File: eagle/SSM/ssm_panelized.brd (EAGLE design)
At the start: 73 x 33.6 mm, 23 parts, among them IC1 4051N, IC2 MCP604P

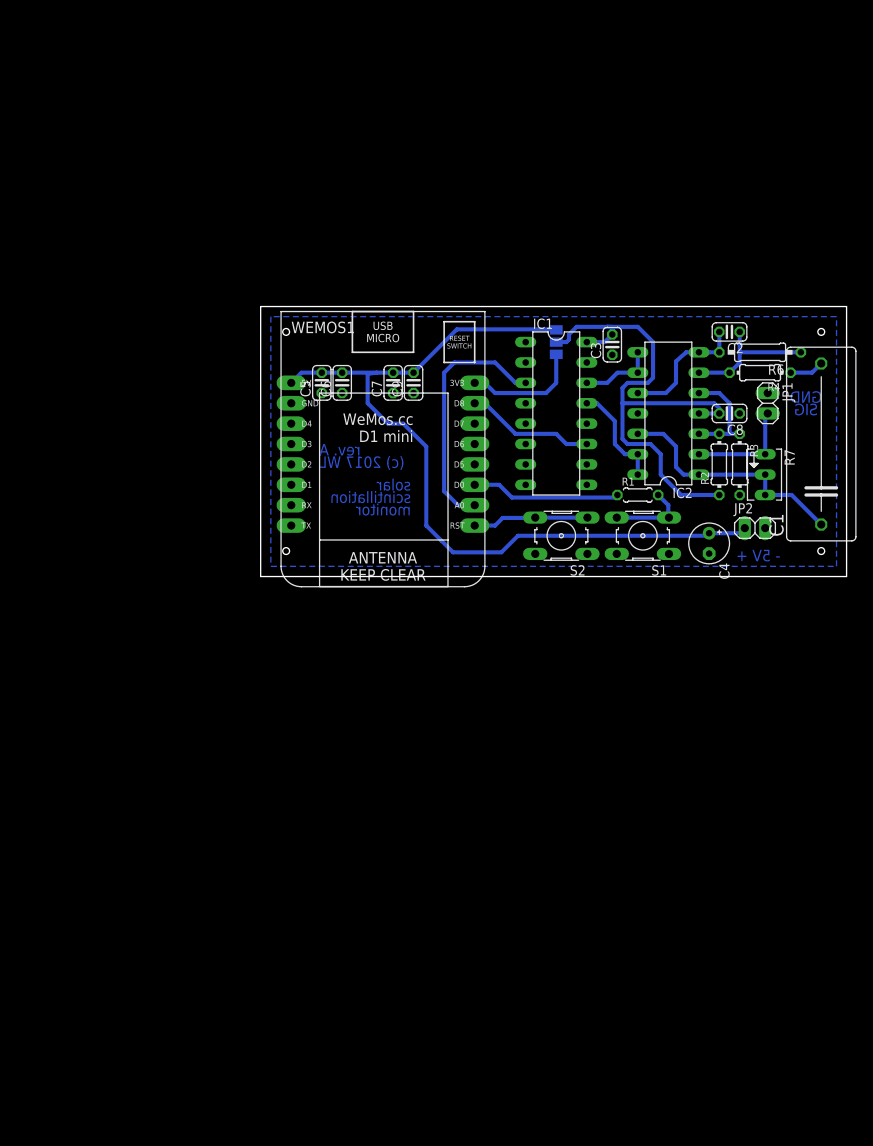
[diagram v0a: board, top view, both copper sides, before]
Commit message: panelized version
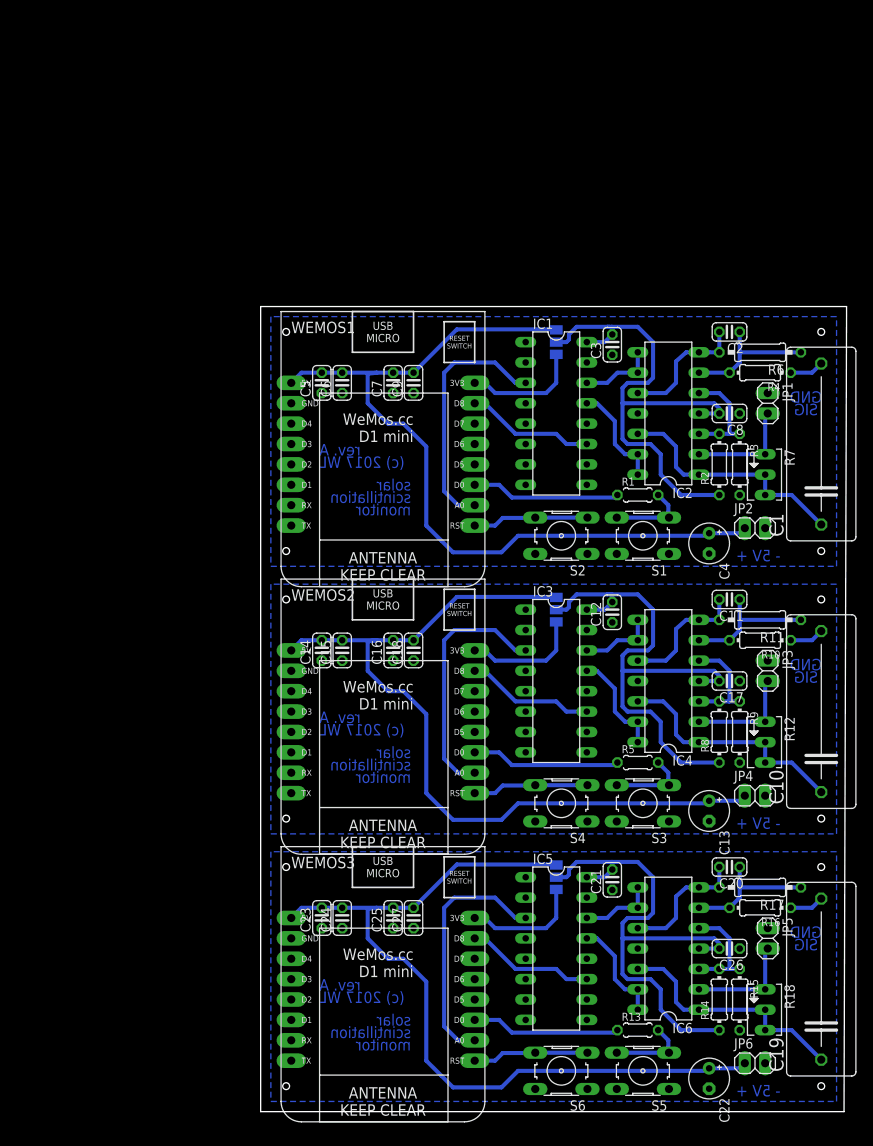
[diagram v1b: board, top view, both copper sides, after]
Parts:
- added C10, C19: 3.3u, Cap:C225-087X210
- added C11, C14, C20, C23: 20p, rcl:C025-024X044
- added C12, C15, C16, C17, C18, C21, C24, C25, C26, C27: 120p, rcl:C025-024X044
- added C13, C22: 470u, rcl:E2,5-5
- added IC3, IC5: 4051N, 40xx:DIL16
- added IC4, IC6: MCP604P, linear:DIL14
- added JP3, JP5: SENS, pinhead:1X02
- added JP4, JP6: PWR, pinhead:1X02
- added R10, R16: 47k, resistor:0204/7
- added R11, R17: 20M, rcl:0207/10
- added R12, R18: 1k, pot:B64Y
- added R13, R5: 470, rcl:0204/5
- added R14, R15, R8, R9: 10k, resistor:0204/7
- added S3, S5: FLS, switch-omron:B3F-10XX
- added S4, S6: RST, switch-omron:B3F-10XX
- added SJ2, SJ3: V, jumper:SJ_2
- added WEMOS2, WEMOS3: NODEMCU, esp8266modules:WEMOS-D1-MINI
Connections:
- new net +3V1: SJ2.1, WEMOS2.3V3
- new net +3V2: SJ3.1, WEMOS3.3V3
- new net +5V1: C13.+, C14.2, C15.2, C16.2, C18.2, JP4.1, SJ2.3, WEMOS2.5V
- new net +5V2: C22.+, C23.2, C24.2, C25.2, C27.2, JP6.1, SJ3.3, WEMOS3.5V
- new net A1: IC3.3, WEMOS2.A0
- new net A2: IC5.3, WEMOS3.A0
- new net D1: R5.1, WEMOS2.D0
- new net D2: R13.1, WEMOS3.D0
- new net GND1: C12.1, C13.-, C14.1, C15.1, C16.1, C17.1, C18.1, IC3.10, IC3.6, IC3.7, IC3.8, IC3.9, IC4.11, JP3.1, JP4.2, R9.2, S3.1, S3.2, S4.1, S4.2, WEMOS2.D5, WEMOS2.GND
- new net GND2: C21.1, C22.-, C23.1, C24.1, C25.1, C26.1, C27.1, IC5.10, IC5.6, IC5.7, IC5.8, IC5.9, IC6.11, JP5.1, JP6.2, R15.2, S5.1, S5.2, S6.1, S6.2, WEMOS3.D5, WEMOS3.GND
- new net N$1: R5.2, S3.3, S3.4
- new net N$10: IC4.2, JP3.2, R12.E
- new net N$11: C10.1, IC4.1, IC4.12, R12.A, R12.S
- new net N$12: C10.2, R10.1
- new net N$13: C11.1, IC4.6, R10.2, R11.1
- new net N$14: C11.2, IC4.10, IC4.7, R11.2
- new net N$15: R13.2, S5.3, S5.4
- new net N$16: IC6.3, IC6.5, R14.2, R15.1
- new net N$17: IC6.2, JP5.2, R18.E
- new net N$18: C19.1, IC6.1, IC6.12, R18.A, R18.S
- new net N$19: C19.2, R16.1
- new net N$20: C20.1, IC6.6, R16.2, R17.1
- new net N$21: C20.2, IC6.10, IC6.7, R17.2
- new net N$9: IC4.3, IC4.5, R8.2, R9.1
- new net NRST1: S4.3, S4.4, WEMOS2.RESET
- new net NRST2: S6.3, S6.4, WEMOS3.RESET
- new net SEL1: IC3.11, WEMOS2.D8
- new net SEL2: IC5.11, WEMOS3.D8
- new net SIG3: IC3.13, IC4.13, IC4.14
- new net SIG4: IC3.14, IC4.8, IC4.9
- new net SIG5: IC5.13, IC6.13, IC6.14
- new net SIG6: IC5.14, IC6.8, IC6.9
- new net VCC1: C12.2, C17.2, IC3.16, IC4.4, R8.1, SJ2.2
- new net VCC2: C21.2, C26.2, IC5.16, IC6.4, R14.1, SJ3.2
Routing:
- net +5V2: track 0.00 -> 102.3 mm
- net +5V1: track 0.00 -> 102.3 mm
- net VCC1: track 0.00 -> 65.7 mm
- net VCC2: track 0.00 -> 65.7 mm
- net A1: track 0.00 -> 31.0 mm
- net A2: track 0.00 -> 31.0 mm
- net N$18: track 0.00 -> 30.5 mm
- net N$11: track 0.00 -> 30.5 mm
- net N$21: track 0.00 -> 18.9 mm
- net N$14: track 0.00 -> 18.9 mm
- net D2: track 0.00 -> 18.6 mm
- net D1: track 0.00 -> 18.6 mm
- net N$20: track 0.00 -> 17.1 mm
- net N$13: track 0.00 -> 17.1 mm
- net SEL1: track 0.00 -> 16.1 mm
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- added copper zone on layer 16, net GND1
- added copper zone on layer 16, net GND2
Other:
- board size 73 x 33.6 mm -> 73 x 100.3 mm

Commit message: move panels to 0,0
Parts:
- moved C11 47.3 mm to (58.4, 63.8)
- moved C5 47.3 mm to (7.62, 90.8)
- moved C6 47.3 mm to (10.2, 90.8)
- moved C7 47.3 mm to (16.5, 90.8)
- moved C8 47.3 mm to (58.4, 87.0)
- moved C9 47.3 mm to (19.1, 90.8)
- moved IC1 47.3 mm to (36.8, 87.0)
- moved IC2 47.3 mm to (50.8, 87.0)
- moved SJ1 47.3 mm to (36.8, 95.9)
- moved C1 47.3 mm to (69.8, 84.5)
- moved C10 47.3 mm to (69.8, 51.1)
- moved C13 47.3 mm to (55.9, 37.5)
- moved C14 47.3 mm to (7.62, 57.5)
- moved C15 47.3 mm to (10.2, 57.5)
- moved C16 47.3 mm to (16.5, 57.5)
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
